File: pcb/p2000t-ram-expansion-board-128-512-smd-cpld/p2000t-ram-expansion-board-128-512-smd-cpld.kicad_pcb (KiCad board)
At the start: 2 copper layers, 110 x 45.5 mm, 20 parts, among them J1 EXPANSION BOARD, J2 POWER, J3 TERMINAL, J4 Atmel-JTAG-10, U1 ATF1502ASV, U2 62128, U3 62128, U4 62128, U5 62128

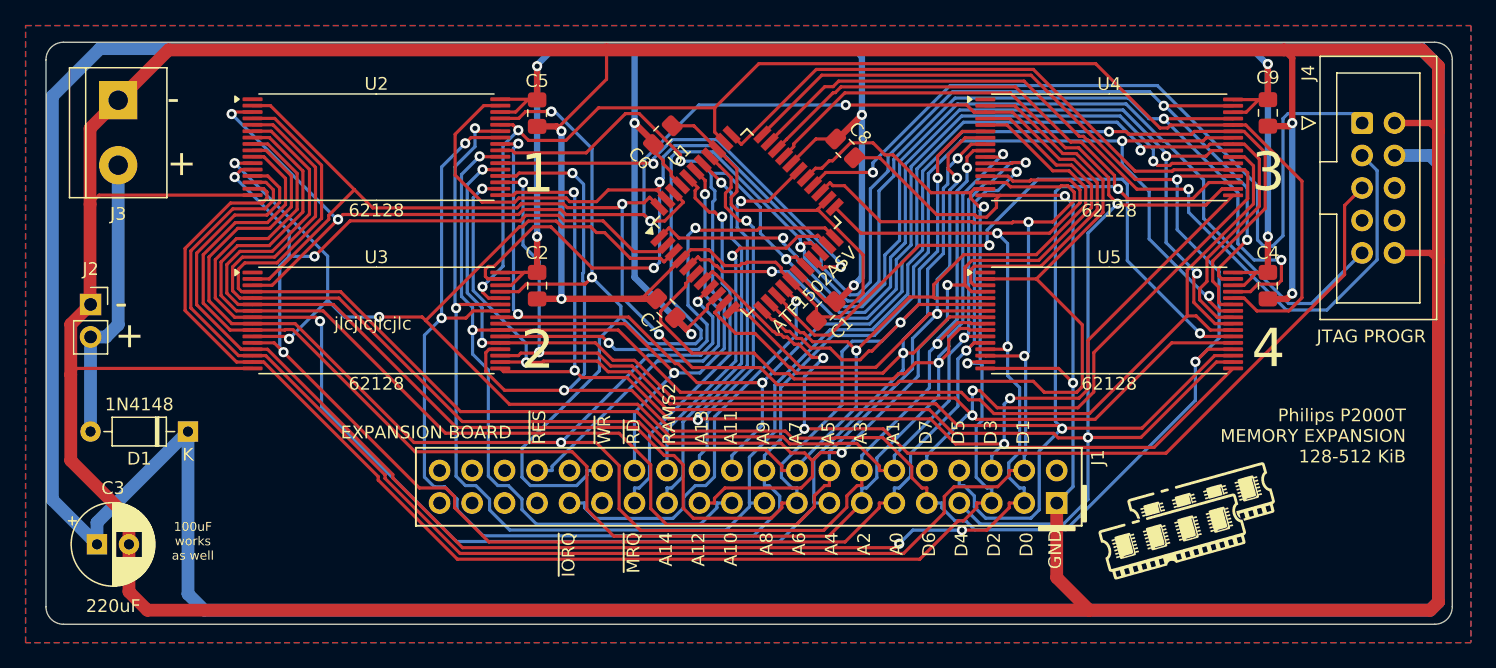
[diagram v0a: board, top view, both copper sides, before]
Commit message: Fixing CUPL code for multi-ram
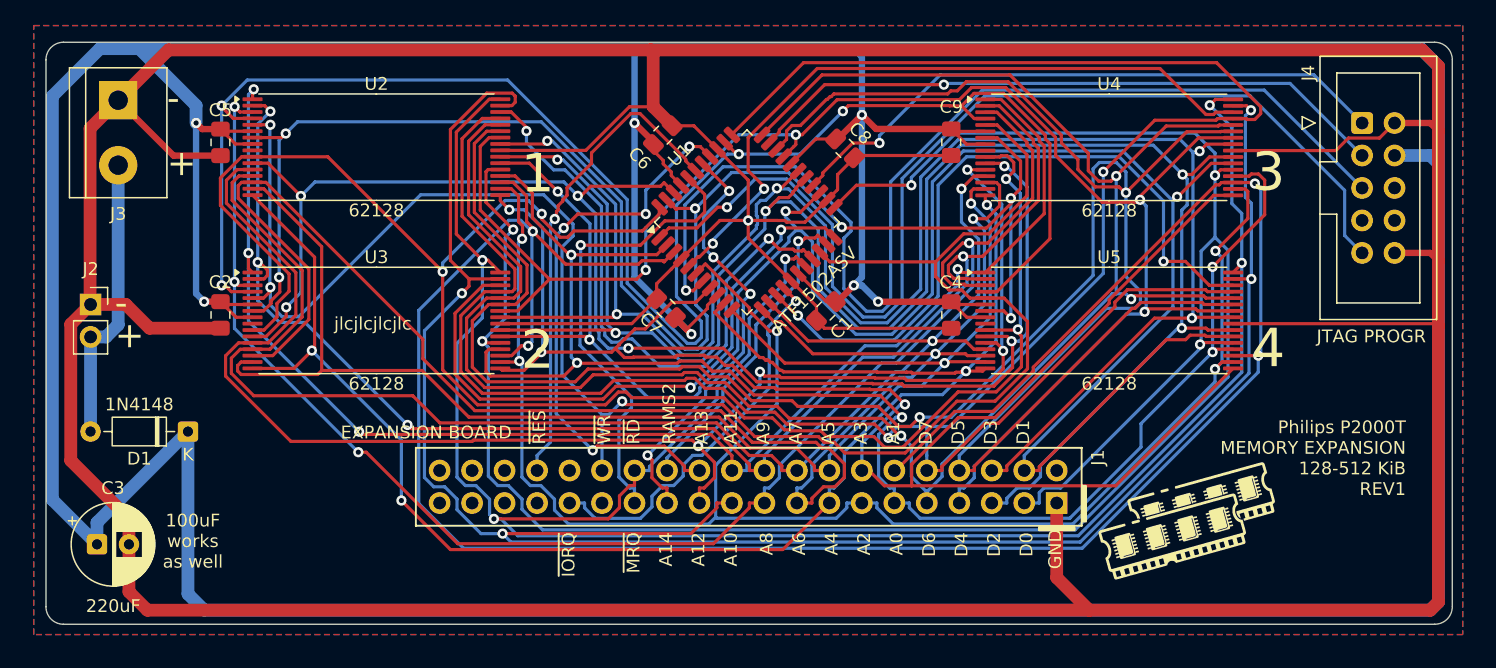
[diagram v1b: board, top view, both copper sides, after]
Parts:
- moved C4 24.9 mm to (90.8, 65.8)
- moved C9 24.9 mm to (90.8, 52.3)
- moved C2 24.9 mm to (33.7, 65.8)
- moved C5 24.9 mm to (33.7, 52.3)
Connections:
- U2 pad 1: unconnected-(U2-NC-Pad1) -> A11
- U2 pad 10: A2 -> R3
- U2 pad 11: A1 -> R1
- U2 pad 12: A0 -> A12
- U2 pad 13: D0 -> A7
- U2 pad 14: D1 -> A6
- U2 pad 15: D2 -> A5
- U2 pad 16: GND -> A4
- U2 pad 17: D3 -> A3
- U2 pad 18: D4 -> A2
- U2 pad 19: D5 -> A1
- U2 pad 2: R3 -> A9
- U2 pad 20: D6 -> A0
- U2 pad 21: D7 -> D0
- U2 pad 22: ~{CS1} -> D1
- U2 pad 23: A10 -> D2
- U2 pad 24: ~{RD} -> GND
- U2 pad 25: A11 -> D3
- U2 pad 26: A9 -> D4
- U2 pad 27: A8 -> D5
- U2 pad 28: R0 -> D6
- U2 pad 29: ~{WR} -> D7
- U2 pad 3: R1 -> A8
- U2 pad 30: +5V -> ~{CS1}
- U2 pad 31: R2 -> A10
- U2 pad 32: +5V -> ~{RD}
- U2 pad 4: A12 -> R0
- U2 pad 5: A7 -> ~{WR}
- U2 pad 6: A6 -> +5V
- U2 pad 7: A5 -> R2
- U2 pad 8: A4 -> +5V
- U2 pad 9: A3 -> unconnected-(U2-NC-Pad9)
- U3 pad 1: unconnected-(U3-NC-Pad1) -> A11
- U3 pad 10: A2 -> R3
- U3 pad 11: A1 -> R1
- U3 pad 12: A0 -> A12
- U3 pad 13: D0 -> A7
- U3 pad 14: D1 -> A6
- U3 pad 15: D2 -> A5
- U3 pad 16: GND -> A4
- U3 pad 17: D3 -> A3
- U3 pad 18: D4 -> A2
- U3 pad 19: D5 -> A1
- U3 pad 2: R3 -> A9
- U3 pad 20: D6 -> A0
- U3 pad 21: D7 -> D0
- U3 pad 22: ~{CS2} -> D1
- U3 pad 23: A10 -> D2
- U3 pad 24: ~{RD} -> GND
- U3 pad 25: A11 -> D3
- U3 pad 26: A9 -> D4
- U3 pad 27: A8 -> D5
- U3 pad 28: R0 -> D6
- U3 pad 29: ~{WR} -> D7
- U3 pad 3: R1 -> A8
- U3 pad 30: +5V -> ~{CS2}
- U3 pad 31: R2 -> A10
- U3 pad 32: +5V -> ~{RD}
- U3 pad 4: A12 -> R0
- U3 pad 5: A7 -> ~{WR}
- U3 pad 6: A6 -> +5V
- U3 pad 7: A5 -> R2
- U3 pad 8: A4 -> +5V
- U3 pad 9: A3 -> unconnected-(U3-NC-Pad9)
- U4 pad 1: unconnected-(U4-NC-Pad1) -> A11
- U4 pad 10: A2 -> R3
- U4 pad 11: A1 -> R1
- U4 pad 12: A0 -> A12
- U4 pad 13: D0 -> A7
- U4 pad 14: D1 -> A6
- U4 pad 15: D2 -> A5
- U4 pad 16: GND -> A4
- U4 pad 17: D3 -> A3
- U4 pad 18: D4 -> A2
- U4 pad 19: D5 -> A1
- U4 pad 2: R3 -> A9
- U4 pad 20: D6 -> A0
- U4 pad 21: D7 -> D0
- U4 pad 22: ~{CS3} -> D1
- U4 pad 23: A10 -> D2
- U4 pad 24: ~{RD} -> GND
- U4 pad 25: A11 -> D3
- U4 pad 26: A9 -> D4
- U4 pad 27: A8 -> D5
- U4 pad 28: R0 -> D6
- U4 pad 29: ~{WR} -> D7
- U4 pad 3: R1 -> A8
- U4 pad 30: +5V -> ~{CS3}
- U4 pad 31: R2 -> A10
- U4 pad 32: +5V -> ~{RD}
- U4 pad 4: A12 -> R0
- U4 pad 5: A7 -> ~{WR}
- U4 pad 6: A6 -> +5V
- U4 pad 7: A5 -> R2
- U4 pad 8: A4 -> +5V
- U4 pad 9: A3 -> unconnected-(U4-NC-Pad9)
- U5 pad 1: unconnected-(U5-NC-Pad1) -> A11
- U5 pad 10: A2 -> R3
- U5 pad 11: A1 -> R1
- U5 pad 12: A0 -> A12
- U5 pad 13: D0 -> A7
- U5 pad 14: D1 -> A6
- U5 pad 15: D2 -> A5
- U5 pad 16: GND -> A4
- U5 pad 17: D3 -> A3
- U5 pad 18: D4 -> A2
- U5 pad 19: D5 -> A1
- U5 pad 2: R3 -> A9
- U5 pad 20: D6 -> A0
- U5 pad 21: D7 -> D0
- U5 pad 22: ~{CS4} -> D1
- U5 pad 23: A10 -> D2
- U5 pad 24: ~{RD} -> GND
- U5 pad 25: A11 -> D3
- U5 pad 26: A9 -> D4
- U5 pad 27: A8 -> D5
- U5 pad 28: R0 -> D6
- U5 pad 29: ~{WR} -> D7
- U5 pad 3: R1 -> A8
- U5 pad 30: +5V -> ~{CS4}
- U5 pad 31: R2 -> A10
- U5 pad 32: +5V -> ~{RD}
- U5 pad 4: A12 -> R0
- U5 pad 5: A7 -> ~{WR}
- U5 pad 6: A6 -> +5V
- U5 pad 7: A5 -> R2
- U5 pad 8: A4 -> +5V
- U5 pad 9: A3 -> unconnected-(U5-NC-Pad9)
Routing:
- net A1: track 130.8 -> 184.4 mm, vias 5 -> 4
- net GND: track 493.6 -> 457.8 mm, vias 6 -> 1
- net D5: track 160.4 -> 195.1 mm, vias 4 -> 2
- net D0: track 144.9 -> 177.3 mm, vias 4 -> 5
- net R0: track 103.4 -> 134.3 mm, vias 2 -> 4
- net A9: track 143.0 -> 112.3 mm
- net D4: track 157.2 -> 127.8 mm
- net ~{RD}: track 141.2 -> 167.1 mm
- net A10: track 131.6 -> 155.5 mm, vias 2 -> 4
- net D7: track 166.8 -> 187.0 mm, vias 4 -> 2
- net A0: track 143.3 -> 123.5 mm
- net TDO: track 68.2 -> 50.7 mm
- net A8: track 138.1 -> 121.0 mm, vias 3 -> 4
- net ~{WR}: track 161.4 -> 144.9 mm, vias 5 -> 3
- net D2: track 133.3 -> 149.1 mm, vias 2 -> 5
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- added copper zone on B.Cu, net +5V
- added copper zone on F.Cu, net GND
- removed copper zone on F.Cu, net (none)
- removed copper zone on B.Cu, net VCC
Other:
- board text added: "Philips P2000T MEMORY EXPANSION 128-512 KiB REV1"
- board text removed: "Philips P2000T MEMORY EXPANSION 128-512 KiB"
